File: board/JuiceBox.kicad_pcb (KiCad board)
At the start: 2 copper layers, 67.2 x 43.8 mm, 38 parts, among them J1 USB_C_Receptacle_USB2.0, SW1 SW_SPST, SW10 SW_SPST, SW11 SW_SPST, SW12 SW_SPST, SW2 SW_SPST, SW3 SW_SPST, SW4 SW_SPST, SW5 SW_SPST, SW6 SW_SPST, SW7 SW_SPST, SW8 SW_SPST, SW9 SW_SPST, U1 ATmega8U2-A, Y1 16MHz

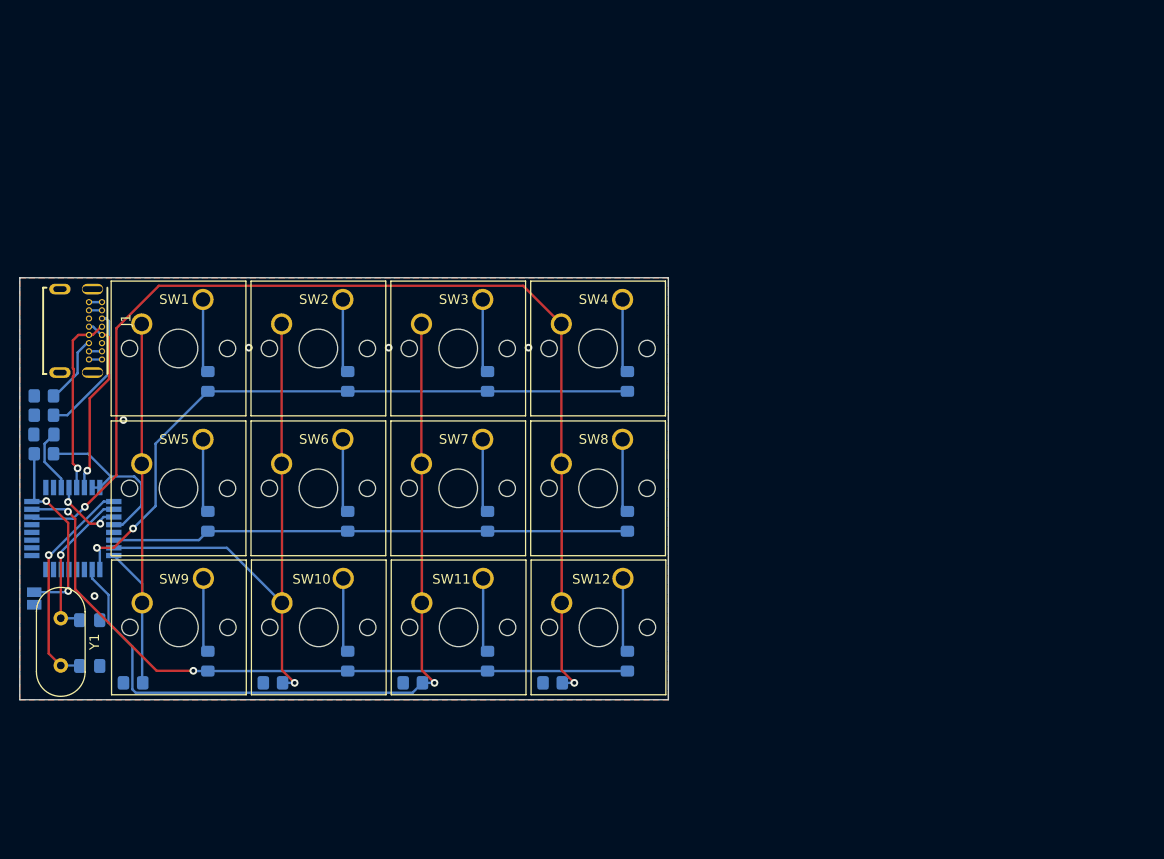
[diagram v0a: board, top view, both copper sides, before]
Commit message: move all components to top, all throughhole
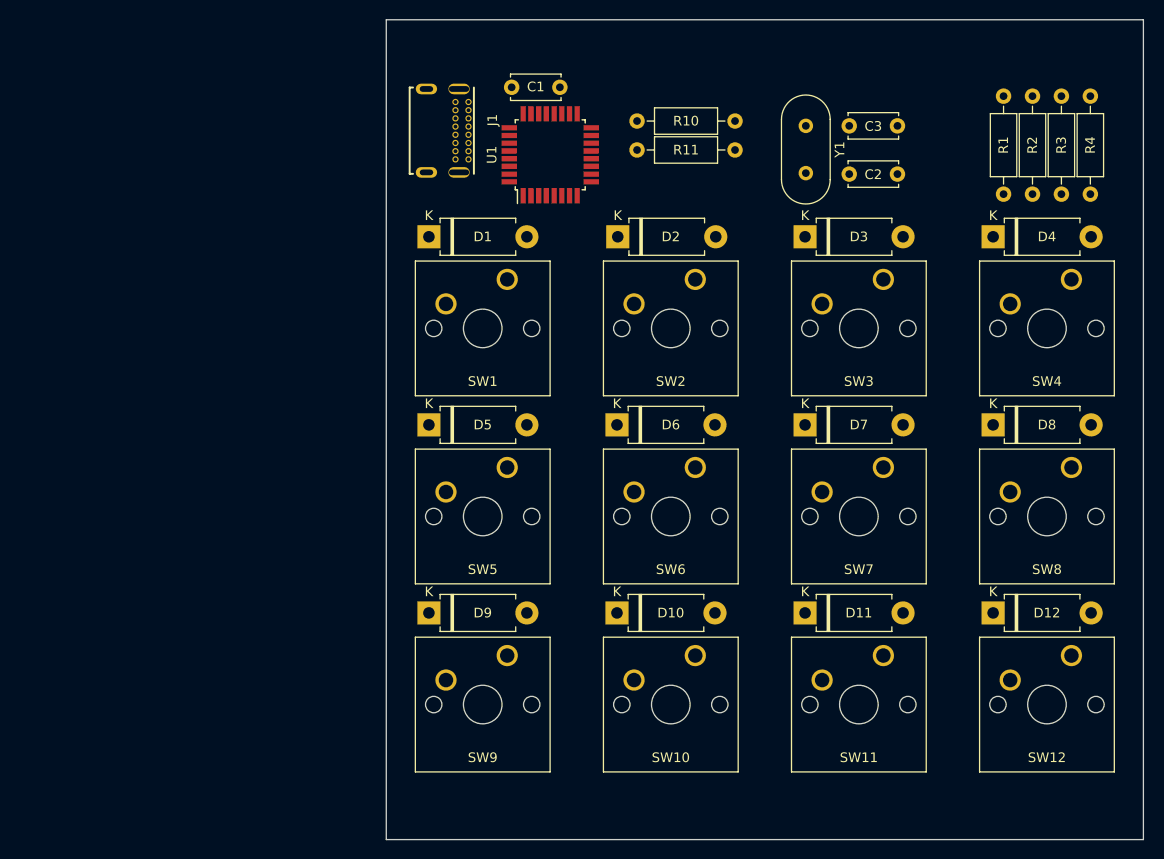
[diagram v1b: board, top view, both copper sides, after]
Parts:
- removed JP1: , Jumper:SolderJumper-2_P1.3mm_Open_Pad1.0x1.5mm
- removed R12: 10K, Resistor_SMD:R_0805_2012Metric_Pad1.20x1.40mm_HandSolder
- C1, C2, C3: footprint Capacitor_SMD:C_0805_2012Metric_Pad1.18x1.45mm_HandSolder -> Capacitor_THT:C_Disc_D5.0mm_W2.5mm_P5.00mm; moved to F.Cu
- D1, D10, D11, D12, D2, D3, D4, D5, D6, D7, D8, D9: footprint Diode_SMD:D_0805_2012Metric_Pad1.15x1.40mm_HandSolder -> Diode_THT:D_DO-15_P10.16mm_Horizontal; moved to F.Cu
- R1, R10, R11, R2, R3, R4: footprint Resistor_SMD:R_0805_2012Metric_Pad1.20x1.40mm_HandSolder -> Resistor_THT:R_Axial_DIN0207_L6.3mm_D2.5mm_P10.16mm_Horizontal; moved to F.Cu
- U1: moved to F.Cu
- moved R1 108.8 mm to (171.0, 37.9), turned to -90 degrees
- moved C3 100.7 mm to (160.0, 41.0)
- moved R2 99.5 mm to (174.0, 37.9), turned to -90 degrees
- moved C2 95.7 mm to (160.0, 46.0)
- moved Y1 95.4 mm to (150.5, 41.0), turned to -90 degrees
- moved R3 90.7 mm to (177.0, 37.9), turned to -90 degrees
- moved R4 82.5 mm to (180.0, 37.9), turned to -90 degrees
- moved R10 68.6 mm to (133.0, 40.5), turned to 0 degrees
- moved R11 66.6 mm to (133.0, 43.5), turned to 0 degrees
- moved C1 64.5 mm to (125.0, 37.0), turned to 180 degrees
- moved U1 62.9 mm to (124.0, 44.0), turned to 90 degrees
- moved SW12 47.2 mm to (178.0, 95.9)
- moved SW8 46.6 mm to (178.0, 76.4)
- moved SW4 46.6 mm to (178.0, 56.9)
- moved J1 43.3 mm to (111.5, 41.5)
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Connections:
- net Net-(J1-PadA6) renamed /D+
- net Net-(J1-PadA7) renamed /D-
- J1 pad P1: GND -> (no net)
- J1 pad P2: GND -> (no net)
- J1 pad P3: GND -> (no net)
- J1 pad P4: GND -> (no net)
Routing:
- net COL_4: track 114.6 -> 0.00 mm, vias 2 -> 0
- net COL_3: track 83.8 -> 0.00 mm, vias 1 -> 0
- net ROW_3: track 73.0 -> 0.00 mm, vias 2 -> 0
- net ROW_1: track 67.9 -> 0.00 mm, vias 2 -> 0
- net COL_2: track 58.8 -> 0.00 mm, vias 1 -> 0
- net ROW_2: track 53.6 -> 0.00 mm
- net COL_1: track 43.4 -> 0.00 mm
- net Net-(C3-Pad2): track 23.0 -> 0.00 mm, vias 1 -> 0
- net +5V: track 21.5 -> 0.00 mm
- net Net-(JP1-Pad2): track 20.5 -> 0.00 mm, vias 2 -> 0
- net /D+: track 19.2 -> 0.00 mm, vias 1 -> 0
- net /D-: track 19.2 -> 0.00 mm, vias 1 -> 0
- net Net-(C2-Pad2): track 16.2 -> 0.00 mm, vias 1 -> 0
- net Net-(J1-PadA5): track 13.8 -> 0.00 mm
- net GND: track 10.4 -> 0.00 mm, vias 7 -> 0
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- removed copper zone on B.Cu, net GND
- removed copper zone on F.Cu, net GND
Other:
- board size 67.2 x 43.8 mm -> 78.5 x 85 mm

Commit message: route pads and throughholes
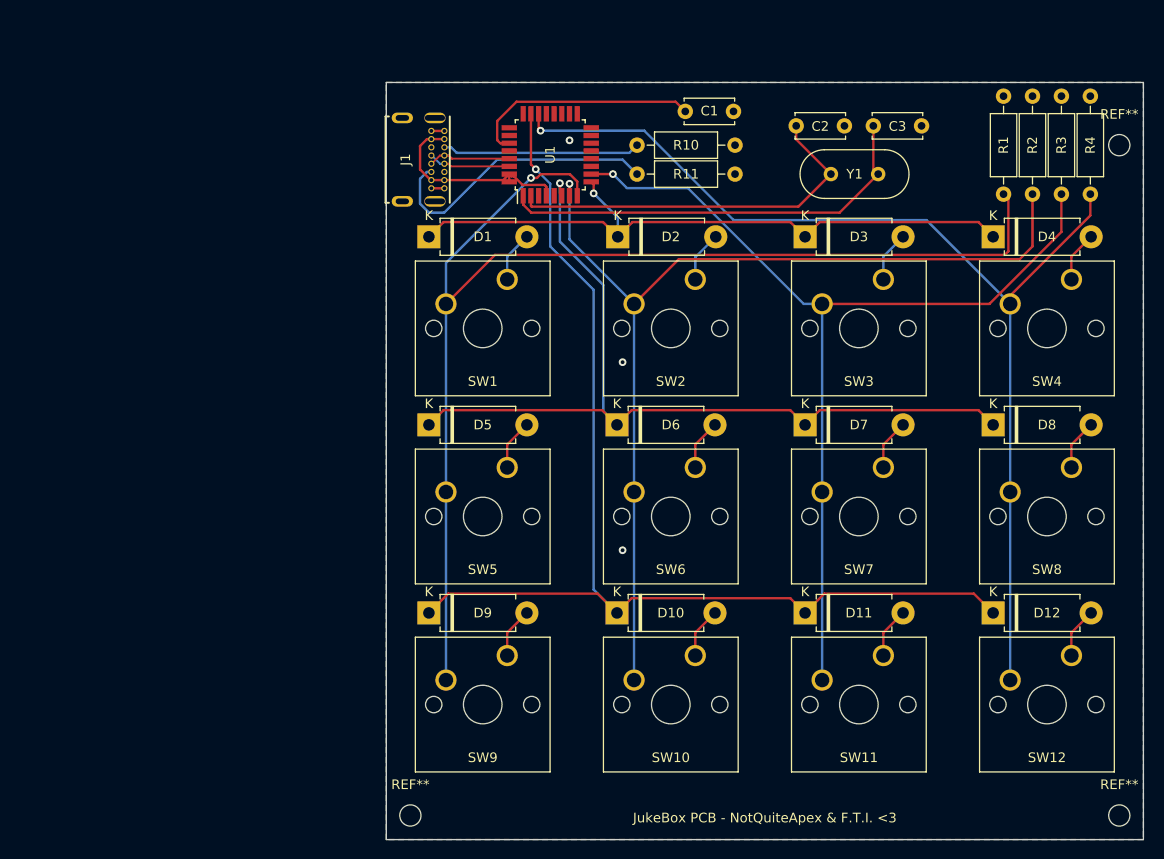
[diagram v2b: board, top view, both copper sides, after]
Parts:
- added REF**: MountingHole_2.2mm_M2, MountingHole:MountingHole_2.2mm_M2, F.Cu at (109.5, 112.5)
- added REF**: MountingHole_2.2mm_M2, MountingHole:MountingHole_2.2mm_M2, F.Cu at (183.0, 43.0)
- added REF**: MountingHole_2.2mm_M2, MountingHole:MountingHole_2.2mm_M2, F.Cu at (183.0, 112.5)
- moved C1 18.2 mm to (143.0, 39.5)
- moved Y1 9.01 mm to (158.0, 46.0), turned to 180 degrees
- moved C2 7.43 mm to (154.5, 41.0)
- moved J1 3.91 mm to (109.0, 44.5)
- moved C3 2.50 mm to (162.5, 41.0)
- moved R10 2.50 mm to (133.0, 43.0)
- moved R11 2.50 mm to (133.0, 46.0)
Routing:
- net COL_1: track 0.00 -> 129.2 mm, vias 0 -> 1
- net ROW_3: track 0.00 -> 118.5 mm, vias 0 -> 1
- net COL_4: track 0.00 -> 111.8 mm, vias 0 -> 1
- net COL_2: track 0.00 -> 104.7 mm, vias 0 -> 1
- net COL_3: track 0.00 -> 100.3 mm, vias 0 -> 1
- net ROW_2: track 0.00 -> 91.2 mm, vias 0 -> 1
- net ROW_1: track 0.00 -> 69.1 mm, vias 0 -> 1
- net Net-(C3-Pad2): track 0.00 -> 44.9 mm
- net Net-(C2-Pad2): track 0.00 -> 40.1 mm
- net Net-(J1-PadB5): track 0.00 -> 29.8 mm
- net Net-(C1-Pad2): track 0.00 -> 24.1 mm
- net +5V: track 0.00 -> 21.3 mm
- net Net-(J1-PadA5): track 0.00 -> 20.5 mm
- net /D+: track 0.00 -> 8.56 mm
- net /D-: track 0.00 -> 8.54 mm
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- added copper zone on B.Cu, net GND
- added copper zone on F.Cu, net GND
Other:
- board size 78.5 x 85 mm -> 78.5 x 78.5 mm
- board text added: "JukeBox PCB - NotQuiteApex & F.T.I. <3"
